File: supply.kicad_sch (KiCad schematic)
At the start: 188 parts, among them IC1 TPS54561, J3 DC_SOCKET, J8 61300311121, Q11 BSS138APW, Q12 BSS138APW, U10 LM3881MME_NOPB, U12 AP62301WU-7, U17 74LVC2G07GV, U18 MAX812REUS+T, U19 PAC1954T-E/4MX, U2 TPS65295RJET, U20 PAC1954T-E/4MX, U21 SN74LVC1G125DBVR, U22 SN74LVC1G125DBVR, U23 SN74LVC1G125DBVR, U24 74LVC2G07GV, U25 NCP718ASN500T1G, U26 MAX16150AUT+T, U27 SN74LVC1G240DCKR, U4 AP62301WU-7, U5 AP62301WU-7, U9 AP62301WU-7

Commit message: Readability improvements
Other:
- moved on the sheet: C149, C152, C155, C156, C157, C158, C174, C182, C183, C215, C216, C218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

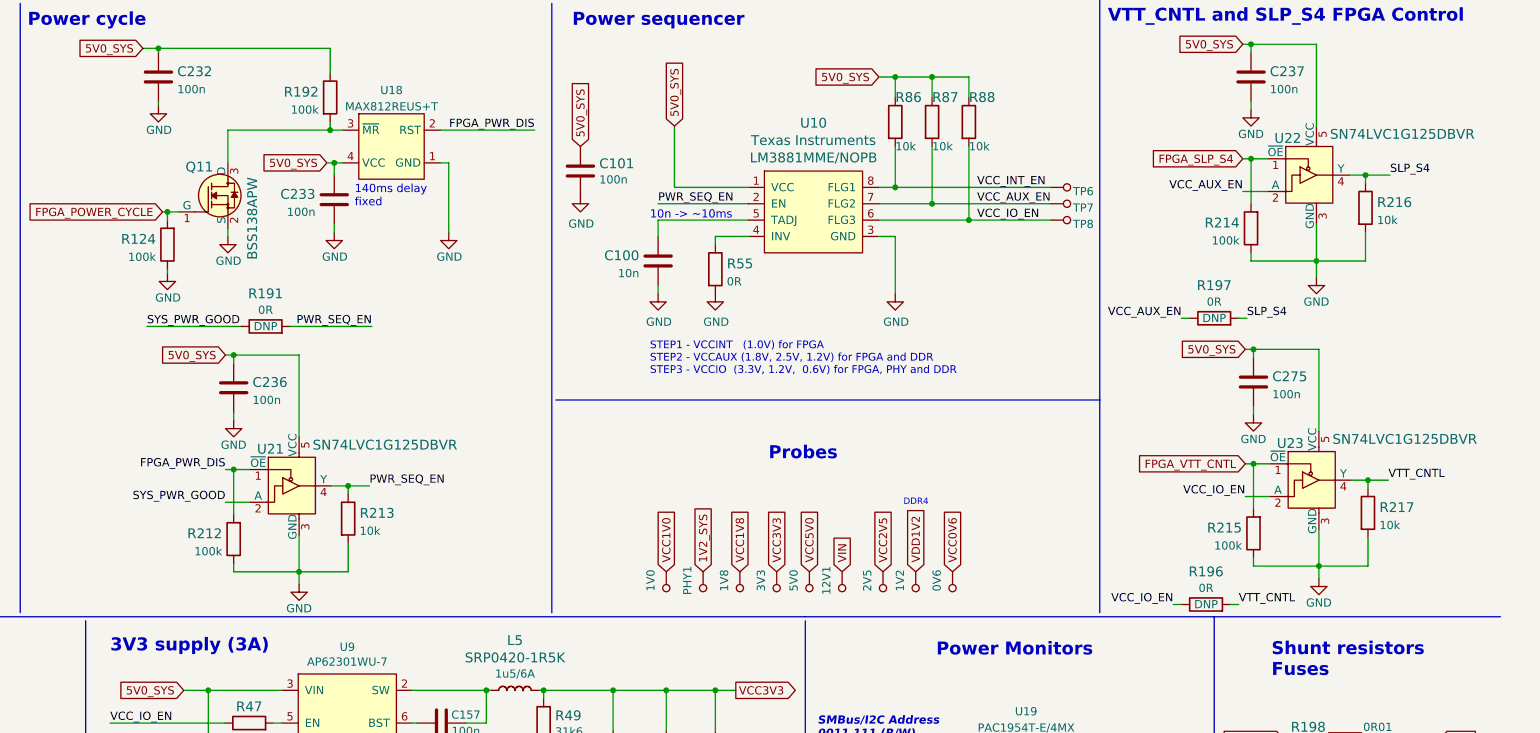
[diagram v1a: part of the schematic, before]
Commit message: Progress in HS matching and deskewing, clear DRC, implement schematic review changes, SI improvments
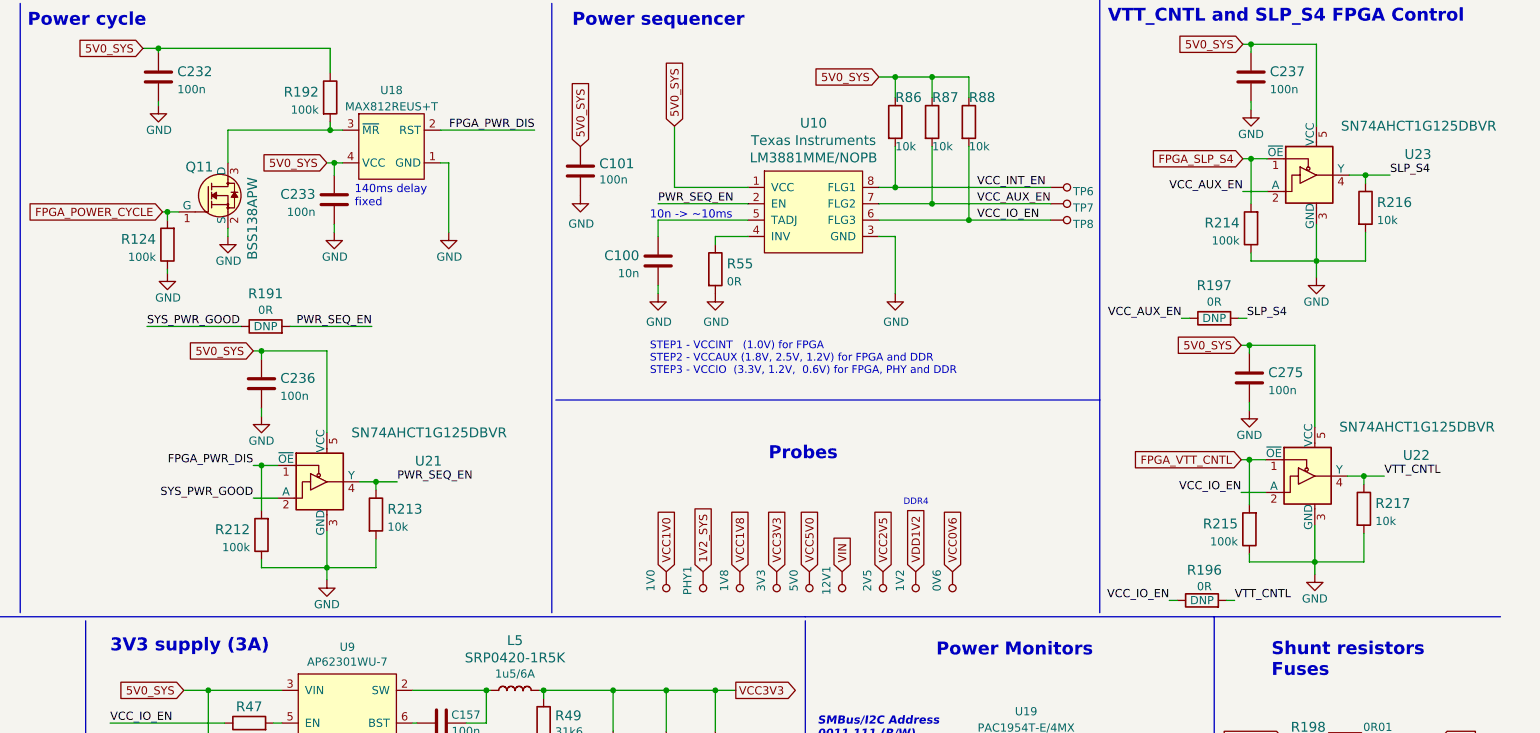
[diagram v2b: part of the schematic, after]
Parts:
- removed U21, U22, U23: SN74LVC1G125DBVR, antmicro-footprints:SOT-753, symbol antmicroLogicBuffersDriversReceiversTransceivers:SN74LVC1G125DBVR
- added U21, U22, U23: SN74AHCT1G125DBVR, antmicro-footprints:SOT-753, symbol antmicroLogicBuffersDriversReceiversTransceivers:SN74AHCT1G125DBVR
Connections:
- net 5V0_SYS: now also U21.5 (VCC), U22.5 (VCC), U23.5 (VCC)
- net FPGA_PWR_DIS: now also U21.1 (~{OE})
- net FPGA_SLP_S4: now also U23.1 (~{OE})
- net FPGA_VTT_CNTL: now also U22.1 (~{OE})
- net GND: now also U21.3 (GND), U22.3 (GND), U23.3 (GND)
- net PWR_SEQ_EN: now also U21.4 (Y)
- net SLP_S4: now also U23.4 (Y)
- net SYS_PWR_GOOD: now also U21.2 (A)
- net VCC_AUX_EN: now also U23.2 (A)
- net VCC_IO_EN: now also U22.2 (A)
- net VTT_CNTL: now also U22.4 (Y)
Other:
- moved on the sheet: C236, C275, R196, R212, R213, R215, R217

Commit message: SI improvments
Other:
- note removed: "To chk: -5V0 sys only to DDR PMIC ? -Power monitors to raw 3V3 instead after fuse?"
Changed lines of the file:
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@@
-    (effects (font (size 1.27 1.27)) (justify left bottom))
-  )
-  (text "To chk:\n-5V0 sys only to DDR PMIC ?\n-Power monitors to raw 3V3 instead after fuse?"
-    (at 1.905 6.985 0)
     (effects (font (size 1.27 1.27)) (justify left bottom))
   )

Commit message: Final touches
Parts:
- added GND1, GND2: RCW-0C, antmicro-footprints:PROBE_PAD_1206, symbol antmicroTestPoints:RCW-0C
- added TP13, TP14: TP_SMD1MM, data-center-dram-tester-footprints:Testpoint_smd_1mm, symbol data-center-dram-tester:TP_SMD1MM
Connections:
- net GND: now also GND1.1, GND2.1
- net at U26.5 (~{INT}): now also TP14.1
- net at U26.6 (~{CLR}): now also TP13.1
- no-connect marks 5 -> 3
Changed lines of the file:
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@@
   )
   (no_connect (at 377.825 240.03))
-  (no_connect (at 140.97 218.44))
-  (no_connect (at 140.97 215.9))
   (no_connect (at 346.71 152.4))
   (no_connect (at 346.71 154.94))
@@
     (stroke (width 0) (type default) (color 0 0 0 0))
   )
+  (wire (pts (xy 146.05 215.9) (xy 146.05 221.615))
+    (stroke (width 0) (type default) (color 0 0 0 0))
+  )
   (wire (pts (xy 111.125 270.51) (xy 112.395 270.51))
     (stroke (width 0) (type default) (color 0 0 0 0))
@@
     (stroke (width 0) (type default) (color 0 0 0 0))
   )
+  (wire (pts (xy 140.97 218.44) (xy 142.24 218.44))
+    (stroke (width 0) (type default) (color 0 0 0 0))
+  )
   (wire (pts (xy 129.54 55.88) (xy 129.54 46.99))
     (stroke (width 0) (type default) (color 0 0 0 0))
@@
     (stroke (width 0) (type default) (color 0 0 0 0))
   )
+  (wire (pts (xy 331.47 86.36) (xy 331.47 87.63))
+    (stroke (width 0) (type default) (color 0 0 0 0))
+  )
   (wire (pts (xy 255.27 264.16) (xy 255.27 267.335))
     (stroke (width 0) (type default) (color 0 0 0 0))
@@
     (stroke (width 0) (type default) (color 0 0 0 0))
   )
+  (wire (pts (xy 140.97 215.9) (xy 146.05 215.9))
+    (stroke (width 0) (type default) (color 0 0 0 0))
+  )
   (wire (pts (xy 144.78 158.75) (xy 152.4 158.75))
     (stroke (width 0) (type default) (color 0 0 0 0))
@@
     (stroke (width 0) (type default) (color 0 0 0 0))
   )
+  (wire (pts (xy 142.24 218.44) (xy 142.24 221.615))
+    (stroke (width 0) (type default) (color 0 0 0 0))
+  )
   (wire (pts (xy 378.841 79.121) (xy 378.841 66.421))
     (stroke (width 0) (type default) (color 0 0 0 0))
@@
     (stroke (width 0) (type default) (color 0 0 0 0))
   )
+  (wire (pts (xy 331.47 99.06) (xy 331.47 100.33))
+    (stroke (width 0) (type default) (color 0 0 0 0))
+  )
   (wire (pts (xy 255.27 264.16) (xy 249.555 264.16))
     (stroke (width 0) (type default) (color 0 0 0 0))
@@
     (pin "2")
   )
+  (symbol (lib_id "antmicroTestPoints:RCW-0C") (at 331.47 96.52 180) (unit 1)
+    (in_bom yes) (on_board yes) (fields_autoplaced)
+    (property "Reference" "GND1" (id 0) (at 332.6638 95.7234 0)
+      (effects (font (size 1.27 1.27)) (justify right))
+    )
+    (property "Value" "RCW-0C" (id 1) (at 332.6638 98.2603 0)
+      (effects (font (size 1.27 1.27)) (justify right))
+    )
+    (property "Footprint" "antmicro-footprints:PROBE_PAD_1206" (id 2) (at 326.39 101.6 0)
+      (effects (font (size 1.524 1.524)) (justify left) hide)
+    )
+    (property "Datasheet" "https://www.te.com/commerce/DocumentDelivery/DDEController?Action=srchrtrv&DocNm=1773266&DocType=DS&DocLang=English" (id 3) (at 326.39 104.14 0)
+      (effects (font (size 1.524 1.524)) (justify left) hide)
+    )
+    (property "MPN" "RCW-0C" (id 4) (at 326.39 109.22 0)
+      (effects (font (size 1.524 1.524)) (justify left) hide)
+    )
+    (property "Manufacturer" "TE Connectivity AMP Connectors" (id 5) (at 326.39 124.46 0)
+      (effects (font (size 1.524 1.524)) (justify left) hide)
+    )
+    (pin "1")
+  )
   (symbol (lib_id "antmicroResistorsmisc:R_0R01_1206") (at 383.54 146.685 0) (unit 1)
     (in_bom yes) (on_board yes)
@@
     (pin "1")
   )
+  (symbol (lib_id "power:GND") (at 331.47 100.33 0) (unit 1)
+    (in_bom yes) (on_board yes)
+    (property "Reference" "#PWR0398" (id 0) (at 331.47 106.68 0)
+      (effects (font (size 1.27 1.27)) hide)
+    )
+    (property "Value" "GND" (id 1) (at 331.47 104.14 0))
+    (property "Footprint" "" (id 2) (at 331.47 100.33 0)
+      (effects (font (size 1.27 1.27)) hide)
+    )
+    (property "Datasheet" "" (id 3) (at 331.47 100.33 0)
+      (effects (font (size 1.27 1.27)) hide)
+    )
+    (pin "1")
+  )
   (symbol (lib_id "antmicroLogicBuffersDriversReceiversTransceivers:SN74AHCT1G125DBVR") (at 225.425 87.63 0) (unit 1)
     (in_bom yes) (on_board yes)
@@
     (pin "5")
   )
+  (symbol (lib_id "power:GND") (at 331.47 87.63 0) (unit 1)
+    (in_bom yes) (on_board yes)
+    (property "Reference" "#PWR0399" (id 0) (at 331.47 93.98 0)
+      (effects (font (size 1.27 1.27)) hide)
+    )
+    (property "Value" "GND" (id 1) (at 331.47 91.44 0))
+    (property "Footprint" "" (id 2) (at 331.47 87.63 0)
+      (effects (font (size 1.27 1.27)) hide)
+    )
+    (property "Datasheet" "" (id 3) (at 331.47 87.63 0)
+      (effects (font (size 1.27 1.27)) hide)
+    )
+    (pin "1")
+  )
   (symbol (lib_id "data-center-dram-tester:GND") (at 317.5 146.05 0) (unit 1)
     (in_bom yes) (on_board yes)
@@
     (pin "6")
   )
+  (symbol (lib_id "data-center-dram-tester:TP_SMD1MM") (at 146.05 224.155 0) (unit 1)
+    (in_bom yes) (on_board yes)
+    (property "Reference" "TP14" (id 0) (at 143.637 222.9612 90))
+    (property "Value" "TP_SMD1MM" (id 1) (at 146.05 226.695 0)
+      (effects (font (size 1.27 1.27)) hide)
+    )
+    (property "Footprint" "data-center-dram-tester-footprints:Testpoint_smd_1mm" (id 2) (at 151.13 219.075 0)
+      (effects (font (size 1.524 1.524)) (justify left) hide)
+    )
+    (property "Datasheet" "" (id 3) (at 151.13 216.535 0)
+      (effects (font (size 1.524 1.524)) (justify left) hide)
+    )
+    (pin "1")
+  )
   (symbol (lib_id "antmicroResistors0603:R_330R_250mW_0603") (at 168.91 262.89 0) (unit 1)
     (in_bom yes) (on_board yes)
@@
     (pin "3")
   )
+  (symbol (lib_id "antmicroTestPoints:RCW-0C") (at 331.47 83.82 180) (unit 1)
+    (in_bom yes) (on_board yes) (fields_autoplaced)
+    (property "Reference" "GND2" (id 0) (at 332.6638 83.0234 0)
+      (effects (font (size 1.27 1.27)) (justify right))
+    )
+    (property "Value" "RCW-0C" (id 1) (at 332.6638 85.5603 0)
+      (effects (font (size 1.27 1.27)) (justify right))
+    )
+    (property "Footprint" "antmicro-footprints:PROBE_PAD_1206" (id 2) (at 326.39 88.9 0)
+      (effects (font (size 1.524 1.524)) (justify left) hide)
+    )
+    (property "Datasheet" "https://www.te.com/commerce/DocumentDelivery/DDEController?Action=srchrtrv&DocNm=1773266&DocType=DS&DocLang=English" (id 3) (at 326.39 91.44 0)
+      (effects (font (size 1.524 1.524)) (justify left) hide)
+    )
+    (property "MPN" "RCW-0C" (id 4) (at 326.39 96.52 0)
+      (effects (font (size 1.524 1.524)) (justify left) hide)
+    )
+    (property "Manufacturer" "TE Connectivity AMP Connectors" (id 5) (at 326.39 111.76 0)
+      (effects (font (size 1.524 1.524)) (justify left) hide)
+    )
+    (pin "1")
+  )
   (symbol (lib_id "data-center-dram-tester:GND") (at 123.19 229.87 0) (unit 1)
     (in_bom yes) (on_board yes)
@@
     )
     (pin "1")
+  )
+  (symbol (lib_id "data-center-dram-tester:TP_SMD1MM") (at 142.24 224.155 0) (unit 1)
+    (in_bom yes) (on_board yes)
+    (property "Reference" "TP13" (id 0) (at 139.827 222.9612 90))
+    (property "Value" "TP_SMD1MM" (id 1) (at 142.24 226.695 0)
+      (effects (font (size 1.27 1.27)) hide)
+    )
+    (property "Footprint" "data-center-dram-tester-footprints:Testpoint_smd_1mm" (id 2) (at 147.32 219.075 0)
+      (effects (font (size 1.524 1.524)) (justify left) hide)
+    )
+    (property "Datasheet" "" (id 3) (at 147.32 216.535 0)
+      (effects (font (size 1.524 1.524)) (justify left) hide)
+    )
+    (pin "1")

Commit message: Add remarks after review to the schenatic
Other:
- note added: "TODO: Add pnp fiducials"
- note added: "TODO: Replace 0R01 with 1206L450SLWR fuse"
- note added: "TODO: Replace TPS54561 with TPS54561QDPRRQ1"
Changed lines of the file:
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@@
     (effects (font (size 1 1)) (justify left bottom))
+  )
+  (text "TODO: Replace TPS54561 with TPS54561QDPRRQ1" (at 424.18 123.19 0)
+    (effects (font (size 1.27 1.27)) (justify left bottom))
   )
   (text "VCC5V0 4.5V to 5.5V" (at 13.97 23.495 0)
@@
     (effects (font (size 1.27 1.27)) (justify left bottom))
   )
+  (text "TODO: Add pnp fiducials" (at 424.18 120.65 0)
+    (effects (font (size 1.27 1.27)) (justify left bottom))
+  )
   (text "Input" (at 128.27 24.13 0)
     (effects (font (size 0.9906 0.9906)) (justify left bottom))
@@
     (effects (font (size 1 1)) (justify left bottom))
   )
+  (text "TODO: Replace 0R01 with 1206L450SLWR fuse" (at 424.18 118.11 0)
+    (effects (font (size 1.27 1.27)) (justify left bottom))
+  )
   (text "Power Monitors" (at 320.04 114.935 0)

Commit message: Fix the remark
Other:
- note added: "TODO: Find Replacement for 0R01"
- note removed: "TODO: Replace 0R01 with 1206L450SLWR fuse"
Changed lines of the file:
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@@
     (effects (font (size 1 1)) (justify left bottom))
   )
-  (text "TODO: Replace 0R01 with 1206L450SLWR fuse" (at 424.18 118.11 0)
+  (text "TODO: Find Replacement for 0R01 " (at 424.18 118.11 0)
     (effects (font (size 1.27 1.27)) (justify left bottom))
   )

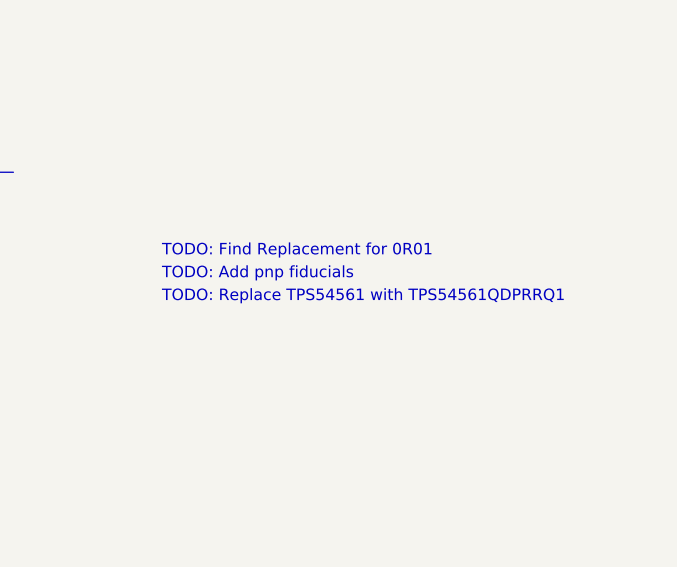
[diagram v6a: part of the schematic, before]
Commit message: DDR SI improvments, optimize bom, apply review issues fix
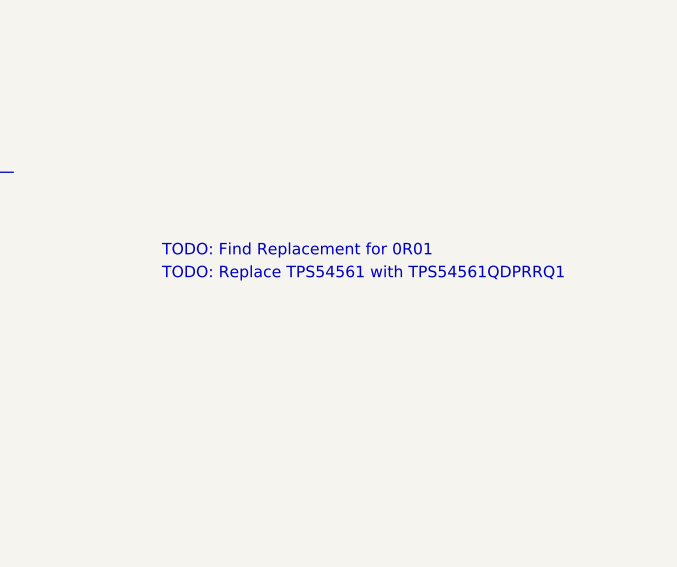
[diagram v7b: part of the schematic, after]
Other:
- note removed: "TODO: Add pnp fiducials"
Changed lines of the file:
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@@
     (effects (font (size 1 1)) (justify left bottom))
   )
-  (text "TODO: Replace TPS54561 with TPS54561QDPRRQ1" (at 424.18 123.19 0)
+  (text "TODO: Replace TPS54561 with TPS54561QDPRRQ1" (at 424.18 120.65 0)
     (effects (font (size 1.27 1.27)) (justify left bottom))
   )
@@
     (effects (font (size 1.27 1.27)) (justify left bottom))
   )
-  (text "TODO: Add pnp fiducials" (at 424.18 120.65 0)
-    (effects (font (size 1.27 1.27)) (justify left bottom))
-  )
